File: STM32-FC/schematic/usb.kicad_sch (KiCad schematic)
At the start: 14 parts, among them J2 USB_C_USB2.0_14P, J3 GH 1.25mm 6P, U2 USBLC6-2SC6, U3 AMS1117-3.3, U4 AMS1117-3.3

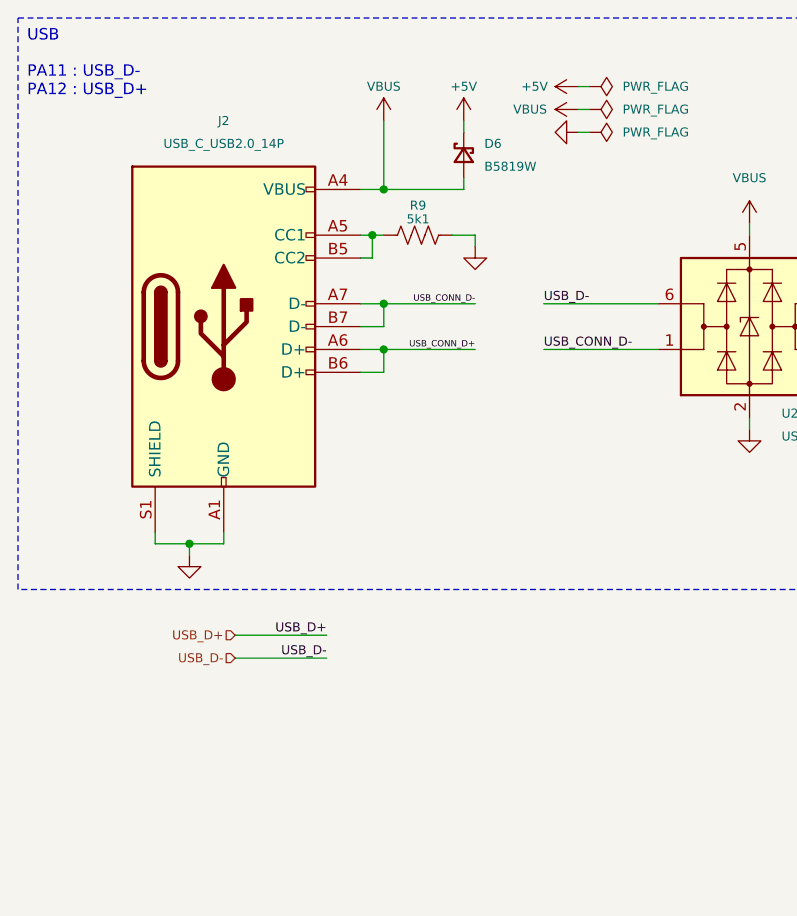
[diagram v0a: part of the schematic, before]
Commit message: v1.0.1 update WIP
repactor and USB C bug fix
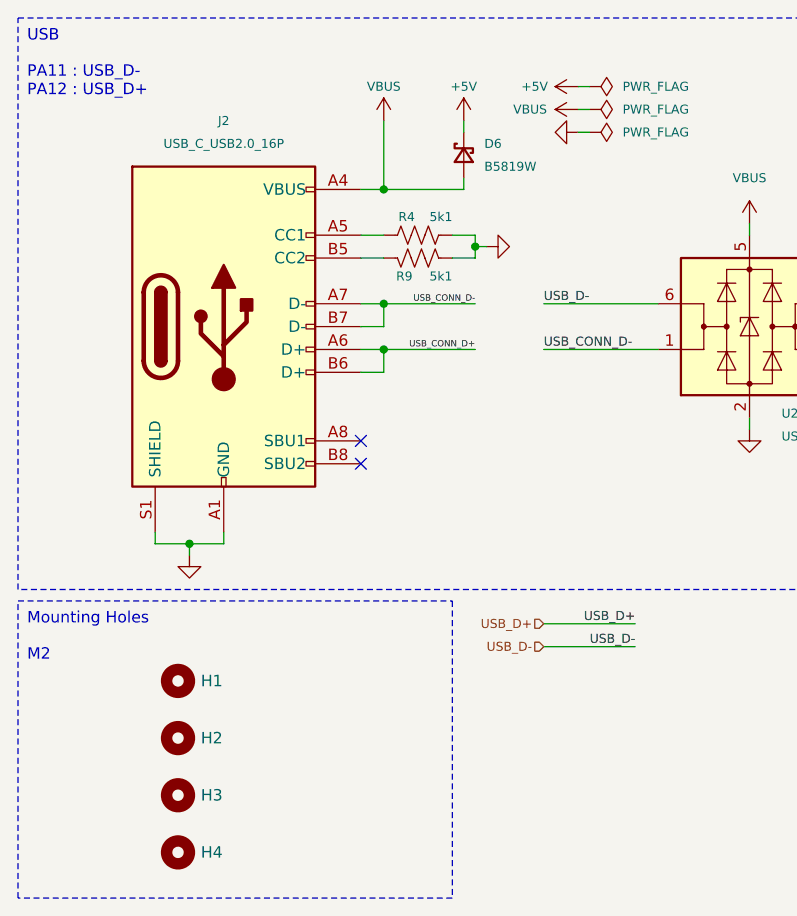
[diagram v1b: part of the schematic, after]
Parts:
- removed J2: USB_C_USB2.0_14P, Connector_USB:USB_C_Receptacle_GCT_USB4110, symbol Connector:USB_C_Receptacle_USB2.0_14P
- added H1, H2, H3, H4: MountingHole, Hole:MountingHole_2.2mm_M2, symbol Mechanical:MountingHole
- added J2: USB_C_USB2.0_16P, Connector_USB:USB_C_Receptacle_GCT_USB4105-xx-A_16P_TopMnt_Horizontal, symbol Connector:USB_C_Receptacle_USB2.0_16P
- added R4: 5k1, Resistor_SMD:R_0402_1005Metric, symbol Device:R_US
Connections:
- net GND: now also J2.A1 (GND), J2.A12 (GND), J2.B1 (GND), J2.B12 (GND), J2.S1 (SHIELD), R4.2
- net USB_CONN_D+: now also J2.A6 (D+), J2.B6 (D+)
- net USB_CONN_D-: now also J2.A7 (D-), J2.B7 (D-)
- net VBUS: now also J2.A4 (VBUS), J2.A9 (VBUS), J2.B4 (VBUS), J2.B9 (VBUS)
- net at R9.1: now also J2.B5 (CC2)
- new net: J2.A5 (CC1), R4.1
- no-connect marks 0 -> 2
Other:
- note added: "M2"
- note added: "Mounting Holes"

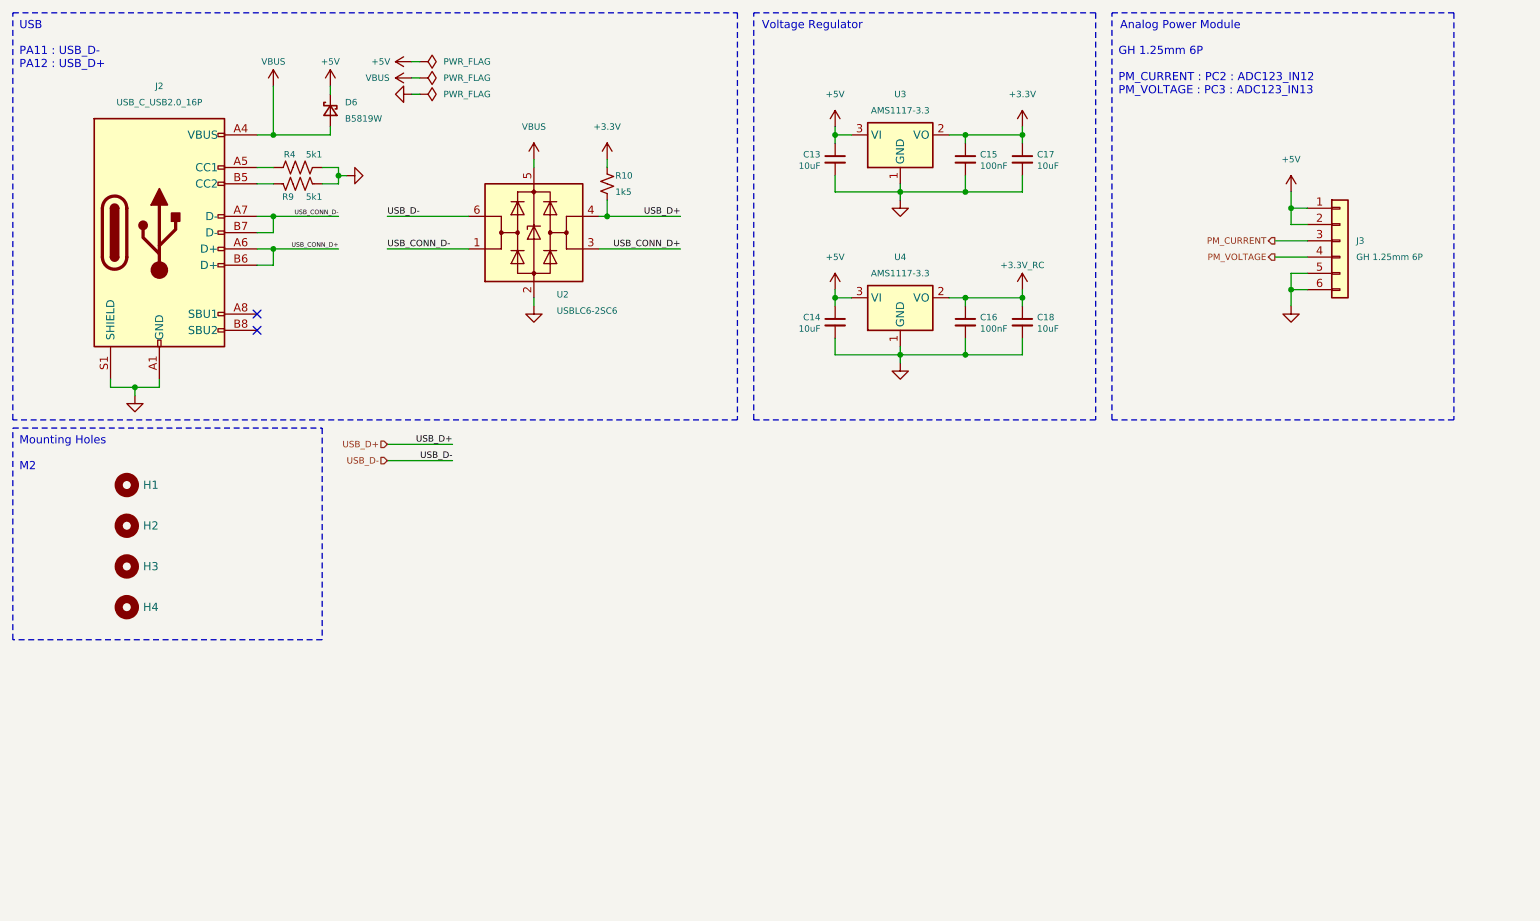
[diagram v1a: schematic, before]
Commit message: schematic update & lib update
- ICM-45686
- ICP-20100
- Micro SD update SDIO instead of SPI
- servo main output
- DC2DC buck instead power regulator
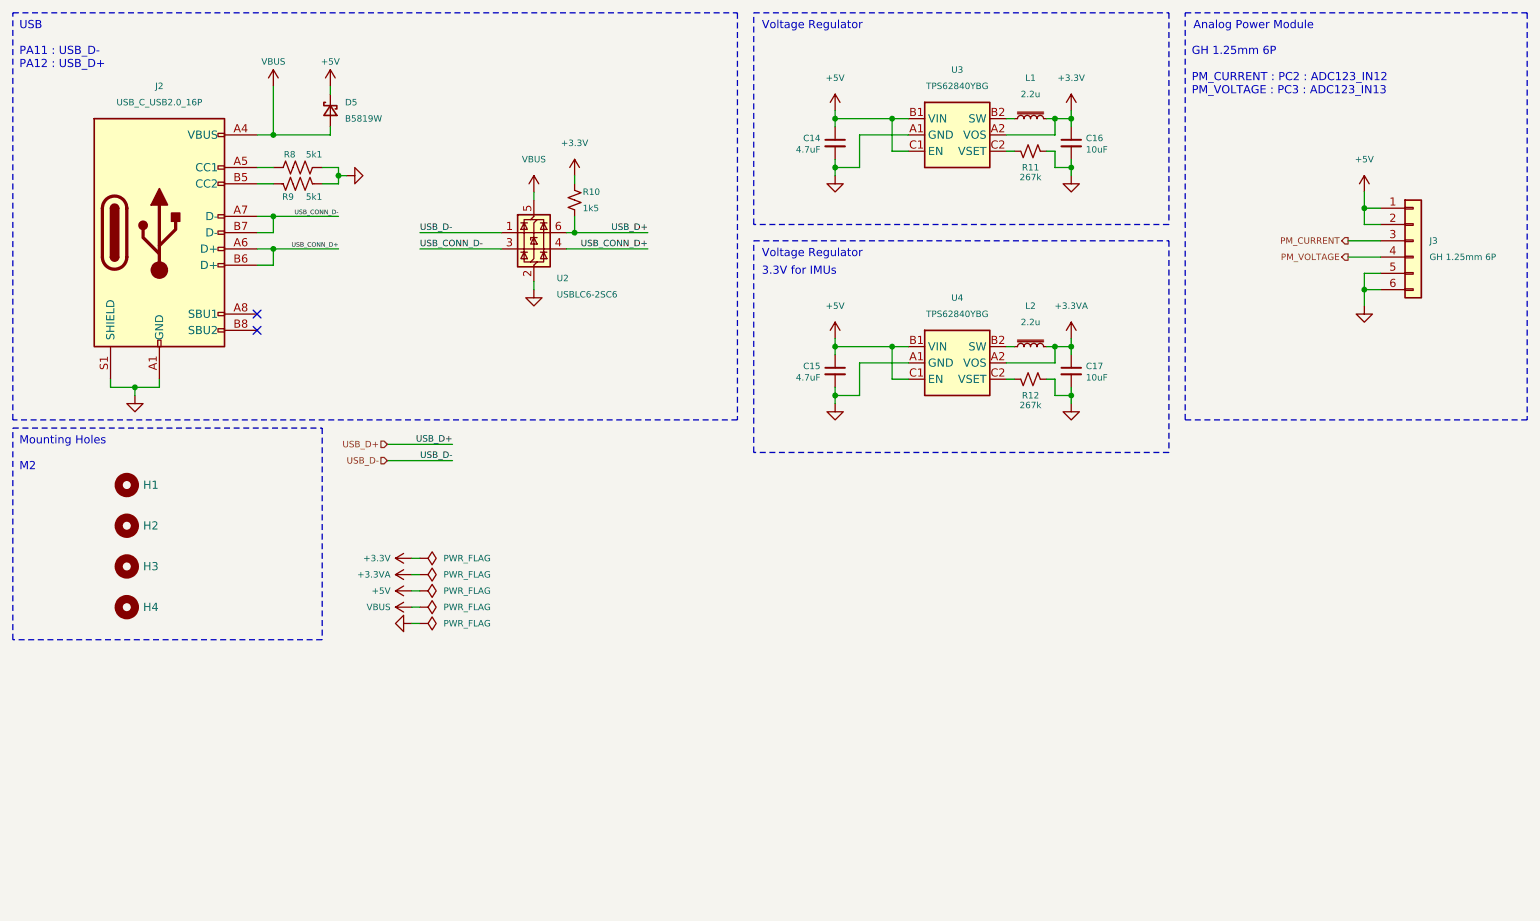
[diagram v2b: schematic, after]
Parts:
- removed C13, C18: 10uF, Capacitor_SMD:C_0402_1005Metric, symbol Device:C_Small
- removed U3, U4: AMS1117-3.3, Package_TO_SOT_SMD:SOT-89-3, symbol Regulator_Linear:AMS1117-3.3
- added L1, L2: 2.2u, VLS201610ET-2R2M:VLS201610ET-2R2M, symbol Device:L_Iron_Small
- added R11, R12: 267k, Resistor_SMD:R_0402_1005Metric, symbol Device:R_Small_US
- added U3, U4: TPS62840YBG, Package_BGA:Texas_DSBGA-6_0.855x1.255mm_Layout2x3_P0.4mm_LevelC, symbol TPS62840:TPS62840YBG
- C14: value 10uF -> 4.7uF; LCSC C77000 -> C307423
- C15: value 100nF -> 4.7uF; LCSC C1525 -> C307423
- C16: value 100nF -> 10uF; LCSC C1525 -> C307415
- C17: LCSC C77000 -> C307415
- H1, H2, H3, H4: footprint Hole:MountingHole_2.2mm_M2 -> MountingHole:MountingHole_2.2mm_M2_Pad
- J3: footprint JST_GH:JST_GH_SM06B-GHS-TB_06x1.25mm_Angled -> Connector_JST:JST_GH_BM06B-GHS-TBT_1x06-1MP_P1.25mm_Vertical; LCSC C133065 -> C189892
- renumbered D6 to D5, R4 to R8
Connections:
- net +3.3V_RC is gone; now on net +3.3V: C16.1
- net +3.3V: now also L1.2, U3.A2 (VOS); no longer C15.1, C17.1
- net +5V: now also C15.1, U3.B1 (VIN), U3.C1 (EN), U4.B1 (VIN), U4.C1 (EN)
- net GND: now also R11.1, R12.1, U3.A1 (GND), U4.A1 (GND)
- net USB_CONN_D+: now also U2.4 (I/O2); no longer U2.3 (I/O2)
- net USB_CONN_D-: now also U2.3 (I/O2); no longer U2.1 (I/O1)
- net USB_D+: now also U2.6 (I/O1); no longer U2.4 (I/O2)
- net USB_D-: now also U2.1 (I/O1); no longer U2.6 (I/O1)
- new net: R11.2, U3.C2 (VSET)
- new net: L2.1, U4.B2 (SW)
- new net: R12.2, U4.C2 (VSET)
- new net: L1.1, U3.B2 (SW)
- new net +3.3VA: C17.1, L2.2, U4.A2 (VOS)
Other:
- note added: "3.3V for IMUs"
- title: STM32 Flight Controller -> NARAEON - Flight Controller
- moved on the sheet: J3, R10

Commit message: add: servo power & comment
- Servo power diode add
- comment update
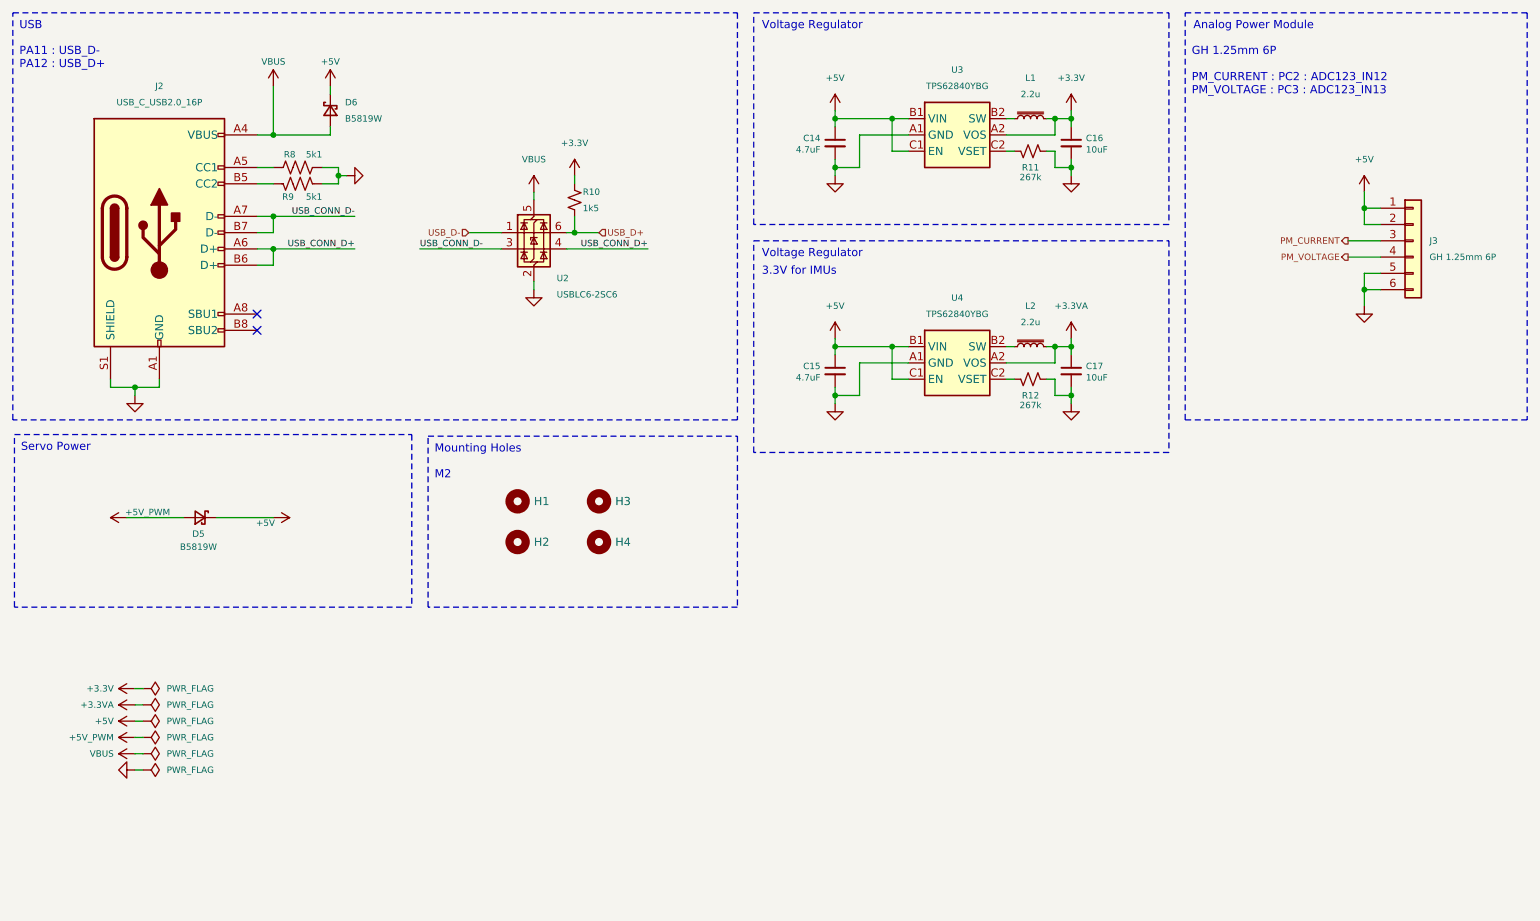
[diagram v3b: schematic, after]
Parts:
- added D5: B5819W, Diode_SMD:D_SOD-323, symbol Device:D_Schottky_Small
- renumbered D5 to D6
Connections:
- net +5V: now also D5.1 (K)
- new net +5V_PWM: D5.2 (A)
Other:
- note added: "Servo Power"
- moved on the sheet: H1, H2, H3, H4

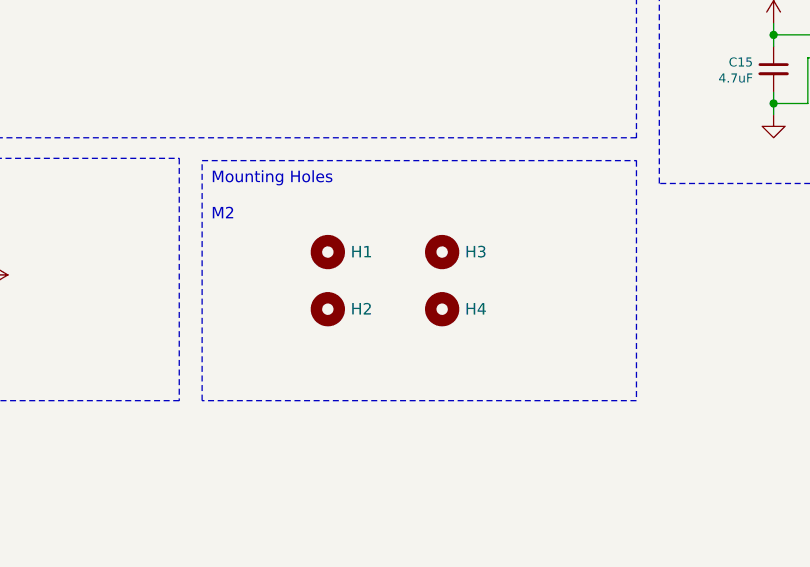
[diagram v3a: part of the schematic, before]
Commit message: update : BJT to MOSFET
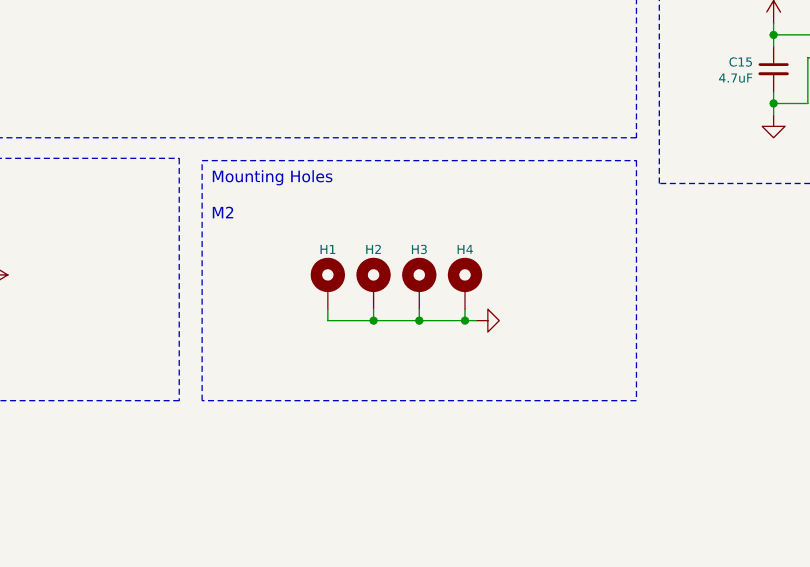
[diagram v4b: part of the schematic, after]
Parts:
- H1, H2, H3, H4: symbol Mechanical:MountingHole -> Mechanical:MountingHole_Pad
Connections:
- net GND: now also H1.1, H2.1, H3.1, H4.1

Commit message: PCB layout done
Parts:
- added JP1: SolderJumper_2_Bridged, Jumper:SolderJumper-2_P1.3mm_Bridged_RoundedPad1.0x1.5mm, symbol Jumper:SolderJumper_2_Bridged
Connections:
- net GND: now also JP1.2 (B)
- new net GNDA: JP1.1 (A)
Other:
- note added: "AHRS"
- note added: "Servo"

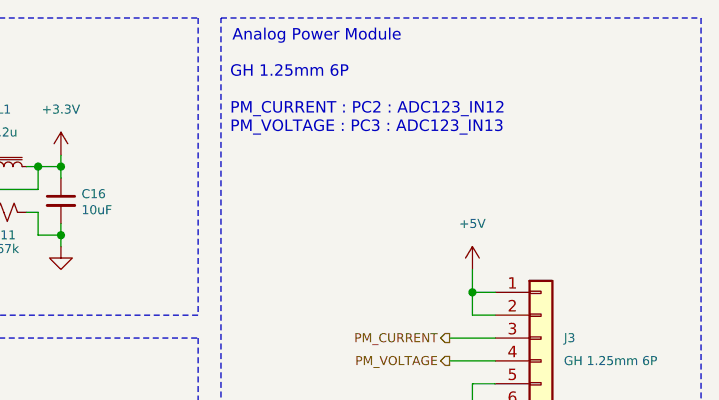
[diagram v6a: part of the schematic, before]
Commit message: fix : readme & schematic minor fix
- schematic comment fix
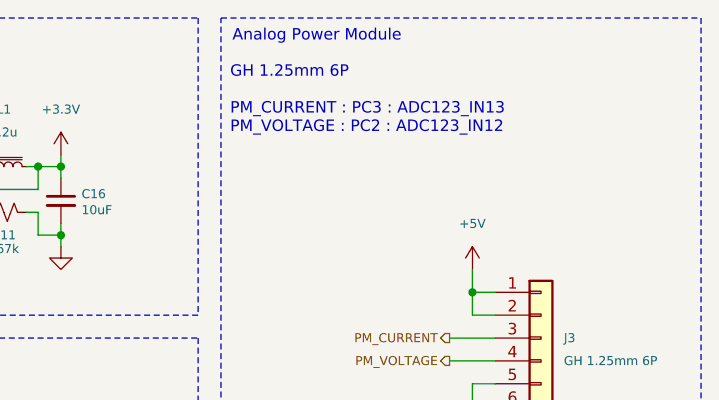
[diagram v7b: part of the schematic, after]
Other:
- note added: "GH 1.25mm 6P PM_CURRENT : PC3 : ADC123_IN13 PM_VOLTAGE : PC2 : ADC123_IN12"
- note removed: "GH 1.25mm 6P PM_CURRENT : PC2 : ADC123_IN12 PM_VOLTAGE : PC3 : ADC123_IN13"
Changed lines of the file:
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@@
 	(title_block
 		(title "NARAEON - Flight Controller")
-		(date "2025-10-10")
+		(date "2025-10-11")
 		(rev "v1.1.0")
 		(company "NARAE")
 		(comment 1 "INHA Univ. Areo-modelling Club")
-		(comment 2 "* Work in progress")
+		(comment 2 "github.com/NARAE-INHA-UNIV")
 	)
 	(rectangle
@@
 		)
 	)
-	(text "GH 1.25mm 6P\n\nPM_CURRENT : PC2 : ADC123_IN12\nPM_VOLTAGE : PC3 : ADC123_IN13"
+	(text "GH 1.25mm 6P\n\nPM_CURRENT : PC3 : ADC123_IN13\nPM_VOLTAGE : PC2 : ADC123_IN12\n"
 		(exclude_from_sim no)
 		(at 206.756 18.034 0)

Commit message: update : Development board
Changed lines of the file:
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@@
-	)
-	(junction
-		(at 185.42 64.77)
-		(diameter 0)
-		(color 0 0 0 0)
 	)
 	(junction
@@
 	(junction
 		(at 233.68 43.18)
-		(diameter 0)
-		(color 0 0 0 0)
-	)
-	(junction
-		(at 185.42 29.21)
 		(diameter 0)
 		(color 0 0 0 0)
@@
 	(wire
 		(pts
-			(xy 184.15 64.77) (xy 185.42 64.77)
+			(xy 184.15 64.77) (xy 187.96 64.77)
 		)
 		(stroke
@@
 	(wire
 		(pts
+			(xy 185.42 31.75) (xy 187.96 29.21)
+		)
+		(stroke
+			(width 0)
+			(type default)
+		)
+	)
+	(wire
+		(pts
 			(xy 231.14 48.26) (xy 236.22 48.26)
 		)
@@
 	(wire
 		(pts
-			(xy 185.42 64.77) (xy 187.96 64.77)
-		)
-		(stroke
-			(width 0)
-			(type default)
-		)
-	)
-	(wire
-		(pts
 			(xy 49.53 139.7) (xy 50.8 139.7)
 		)
@@
 	(wire
 		(pts
-			(xy 185.42 29.21) (xy 187.96 29.21)
-		)
-		(stroke
-			(width 0)
-			(type default)
-		)
-	)
-	(wire
-		(pts
-			(xy 185.42 67.31) (xy 185.42 64.77)
-		)
-		(stroke
-			(width 0)
-			(type default)
-		)
-	)
-	(wire
-		(pts
 			(xy 185.42 36.83) (xy 187.96 36.83)
 		)
@@
 	(wire
 		(pts
+			(xy 185.42 67.31) (xy 187.96 64.77)
+		)
+		(stroke
+			(width 0)
+			(type default)
+		)
+	)
+	(wire
+		(pts
 			(xy 187.96 27.94) (xy 187.96 29.21)
 		)
@@
 	(wire
 		(pts
-			(xy 185.42 31.75) (xy 185.42 29.21)
-		)
-		(stroke
-			(width 0)
-			(type default)
-		)
-	)
-	(wire
-		(pts
 			(xy 86.36 49.53) (xy 99.06 49.53)
 		)
@@
 	(wire
 		(pts
-			(xy 184.15 29.21) (xy 185.42 29.21)
-		)
-		(stroke
+			(xy 184.15 29.21) (xy 187.96 29.21)
+		)
+		(stroke
